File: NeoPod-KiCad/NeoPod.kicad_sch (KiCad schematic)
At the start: 61 parts, among them J1 SJ-3523-SMT-TR, J2 USB4500-03-0-A_REVA1, J4 USB4500-03-0-A_REVA1, Q1 CSD25480F3, SW1 SW_SPST, SW2 SW_SPST, SW3 SW_SPST, SW4 SW_SPST, SW5 SW_SPST, U1 ESP32-WROOM-32, U10 SN74CB3Q3257DBQR, U2 PCM5102A, U3 RP2040, U4 CP2102N-Axx-xQFN24, U5 XC6210B332MR, U6 STC4054GR, U7 TFT_320x240, Y2 40MHz-Xtal

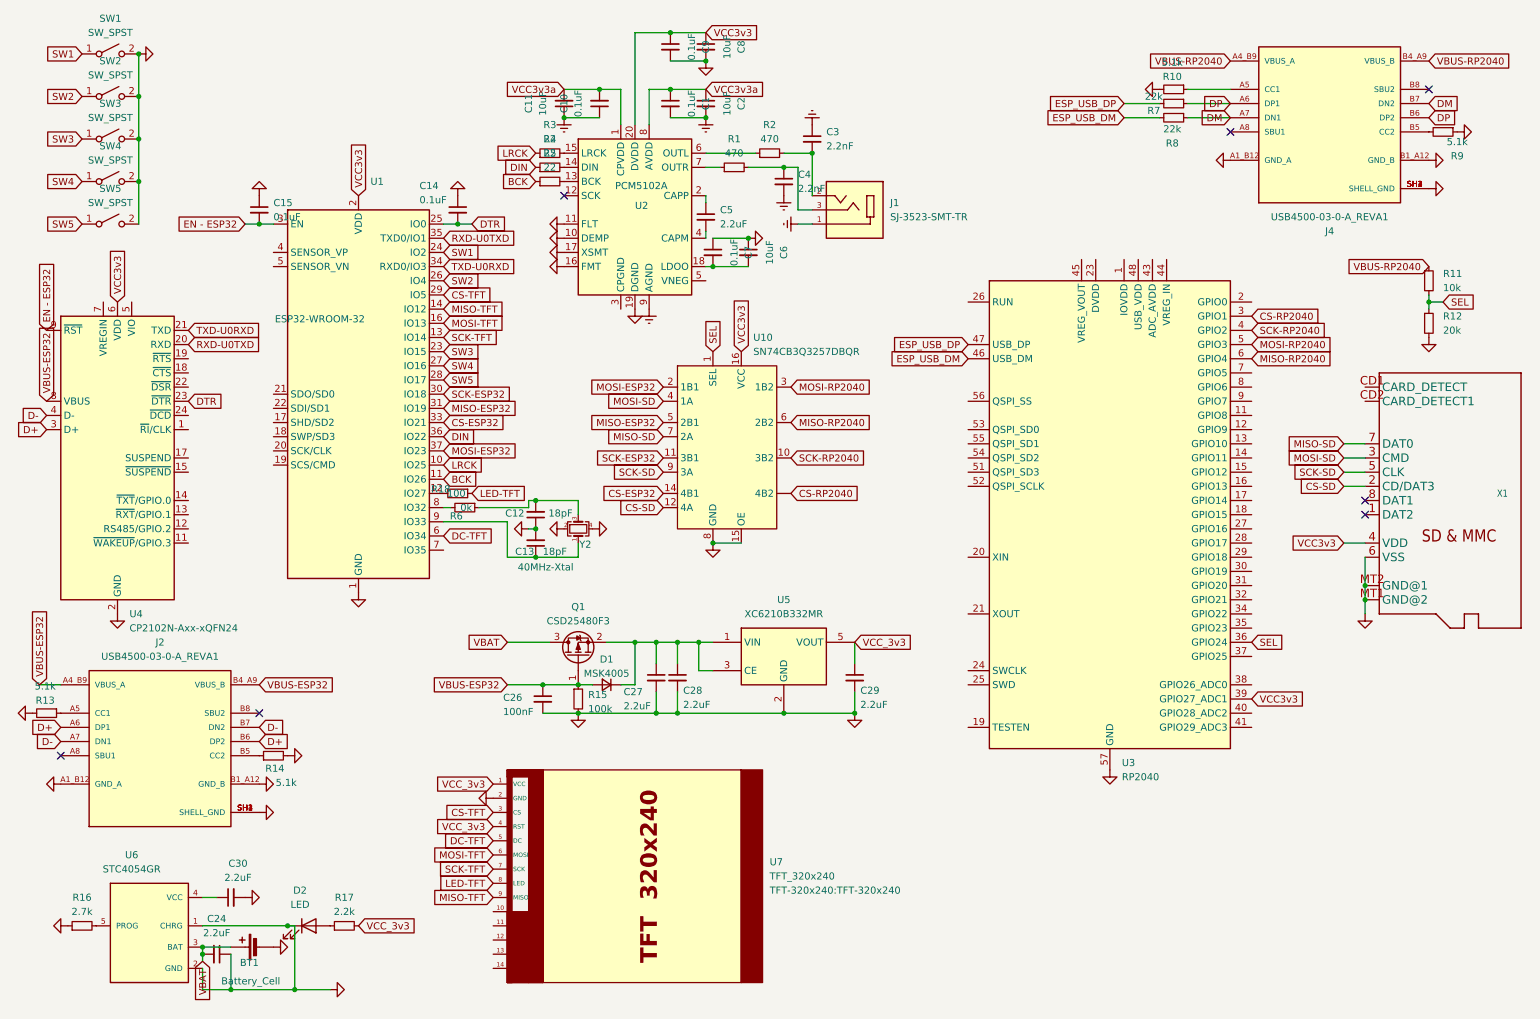
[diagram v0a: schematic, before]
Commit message: Started pcb layout and added images
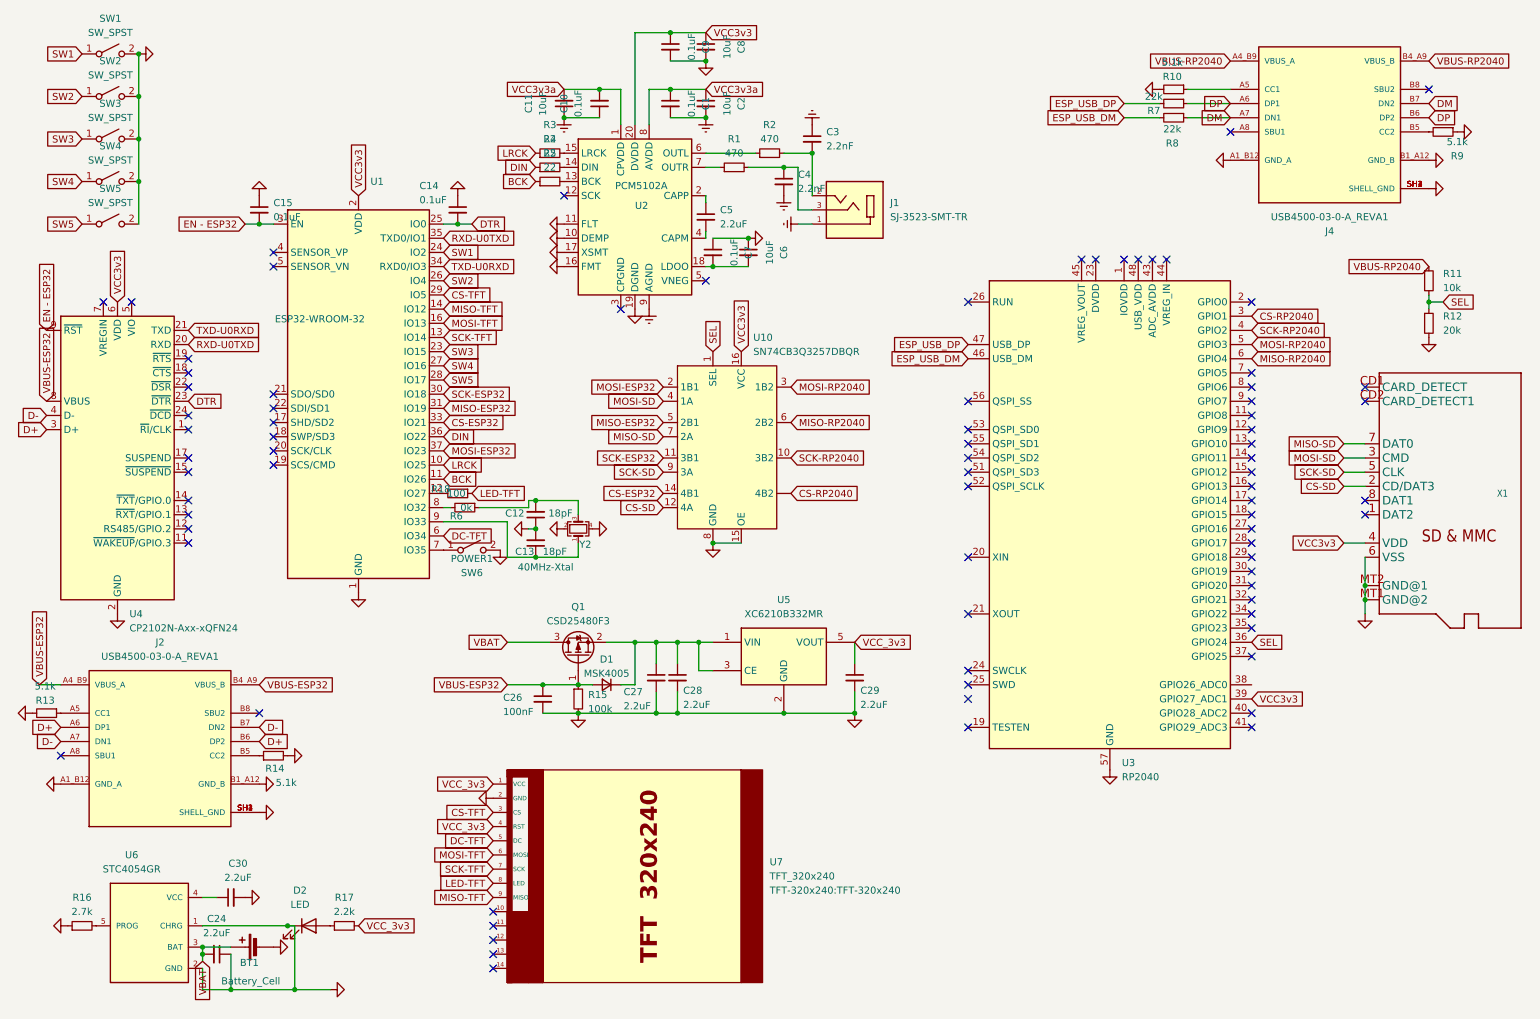
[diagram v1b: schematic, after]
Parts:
- added POWER1: SW6, SW_TS-1088-AR2016:SW_TS-1088-AR02016, symbol Switch:SW_SPST
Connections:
- net AGND: no longer C14.1, C15.1, C6.1, C7.1, J2.A1_B12 (GND_A), J2.B1_A12 (GND_B), J2.SH1 (SHELL_GND), J2.SH2 (SHELL_GND), J2.SH3 (SHELL_GND), J2.SH4 (SHELL_GND), R12.2, SW1.2 (B), SW2.2 (B), SW3.2 (B), SW4.2 (B), SW5.2 (B), U1.1 (GND), U1.15 (GND), U1.38 (GND), U1.39 (GND), U2.10 (DEMP), U2.11 (FLT), U2.16 (FMT), U2.17 (XSMT), U3.57 (GND), U4.2 (GND), U4.25 (GND)
- net GND: now also C14.1, C15.1, C6.1, C7.1, J2.A1_B12 (GND_A), J2.B1_A12 (GND_B), J2.SH1 (SHELL_GND), J2.SH2 (SHELL_GND), J2.SH3 (SHELL_GND), J2.SH4 (SHELL_GND), R12.2, SW1.2 (B), SW2.2 (B), SW3.2 (B), SW4.2 (B), SW5.2 (B), U1.1 (GND), U1.15 (GND), U1.38 (GND), U1.39 (GND), U2.10 (DEMP), U2.11 (FLT), U2.16 (FMT), U2.17 (XSMT), U3.57 (GND), U4.2 (GND), U4.25 (GND), POWER1.2 (B)
- net at U1.7 (IO35): now also POWER1.1 (A)
- no-connect marks 7 -> 79

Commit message: finished pcb
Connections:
- net AGND is gone; now on net GND: C8.2, C9.2, U2.19 (DGND)
- net VCC_3v3 is gone; now on net VCC3v3: C29.1, R17.2, U5.5 (VOUT), U7.1 (VCC), U7.4 (RST)
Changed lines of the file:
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@@
 		)
 	)
+	(global_label "VCC3v3"
+		(shape input)
+		(at 74.93 176.53 0)
+		(fields_autoplaced yes)
+		(effects
+			(font
+				(size 1.27 1.27)
+			)
+			(justify left)
+		)
+		(property "Intersheetrefs" "${INTERSHEET_REFS}"
+			(at 84.9304 176.53 0)
+			(effects
+				(font
+					(size 1.27 1.27)
+				)
+				(justify left)
+				(hide yes)
+			)
+		)
+	)
 	(global_label "VCC3v3a"
 		(shape input)
@@
 		)
 	)
-	(global_label "VCC_3v3"
-		(shape input)
-		(at 163.83 125.73 0)
-		(fields_autoplaced yes)
-		(effects
-			(font
-				(size 1.27 1.27)
-			)
-			(justify left)
-		)
-		(property "Intersheetrefs" "${INTERSHEET_REFS}"
-			(at 174.798 125.73 0)
-			(effects
-				(font
-					(size 1.27 1.27)
-				)
-				(justify left)
-				(hide yes)
-			)
-		)
-	)
 	(global_label "VBUS-ESP32"
 		(shape input)
@@
 		)
 	)
+	(global_label "VCC3v3"
+		(shape input)
+		(at 99.06 158.75 180)
+		(fields_autoplaced yes)
+		(effects
+			(font
+				(size 1.27 1.27)
+			)
+			(justify right)
+		)
+		(property "Intersheetrefs" "${INTERSHEET_REFS}"
+			(at 89.0596 158.75 0)
+			(effects
+				(font
+					(size 1.27 1.27)
+				)
+				(justify right)
+				(hide yes)
+			)
+		)
+	)
 	(global_label "VBAT"
 		(shape input)
@@
 		)
 	)
+	(global_label "VCC3v3"
+		(shape input)
+		(at 99.06 151.13 180)
+		(fields_autoplaced yes)
+		(effects
+			(font
+				(size 1.27 1.27)
+			)
+			(justify right)
+		)
+		(property "Intersheetrefs" "${INTERSHEET_REFS}"
+			(at 89.0596 151.13 0)
+			(effects
+				(font
+					(size 1.27 1.27)
+				)
+				(justify right)
+				(hide yes)
+			)
+		)
+	)
 	(global_label "SW2"
 		(shape input)
@@
 		)
 	)
-	(global_label "VCC_3v3"
-		(shape input)
-		(at 74.93 176.53 0)
-		(fields_autoplaced yes)
-		(effects
-			(font
-				(size 1.27 1.27)
-			)
-			(justify left)
-		)
-		(property "Intersheetrefs" "${INTERSHEET_REFS}"
-			(at 85.898 176.53 0)
-			(effects
-				(font
-					(size 1.27 1.27)
-				)
-				(justify left)
-				(hide yes)
-			)
-		)
-	)
 	(global_label "DP"
 		(shape input)
@@
 		)
 	)
-	(global_label "VCC_3v3"
-		(shape input)
-		(at 99.06 158.75 180)
-		(fields_autoplaced yes)
-		(effects
-			(font
-				(size 1.27 1.27)
-			)
-			(justify right)
-		)
-		(property "Intersheetrefs" "${INTERSHEET_REFS}"
-			(at 88.092 158.75 0)
-			(effects
-				(font
-					(size 1.27 1.27)
-				)
-				(justify right)
-				(hide yes)
-			)
-		)
-	)
 	(global_label "MOSI-SD"
 		(shape input)
@@
 		)
 	)
+	(global_label "VCC3v3"
+		(shape input)
+		(at 163.83 125.73 0)
+		(fields_autoplaced yes)
+		(effects
+			(font
+				(size 1.27 1.27)
+			)
+			(justify left)
+		)
+		(property "Intersheetrefs" "${INTERSHEET_REFS}"
+			(at 173.8304 125.73 0)
+			(effects
+				(font
+					(size 1.27 1.27)
+				)
+				(justify left)
+				(hide yes)
+			)
+		)
+	)
 	(global_label "VBUS-ESP32"
 		(shape input)
@@
 		)
 	)
-	(global_label "VCC_3v3"
-		(shape input)
-		(at 99.06 151.13 180)
-		(fields_autoplaced yes)
-		(effects
-			(font
-				(size 1.27 1.27)
-			)
-			(justify right)
-		)
-		(property "Intersheetrefs" "${INTERSHEET_REFS}"
-			(at 88.092 151.13 0)
-			(effects
-				(font
-					(size 1.27 1.27)
-				)
-				(justify right)
-				(hide yes)
-			)
-		)
-	)
 	(global_label "VCC3v3"
 		(shape input)
@@
 			)
 		)
-		(property "Value" "AGND"
+		(property "Value" "GND"
 			(at 137.16 26.67 0)
 			(effects
@@
 			)
 		)
-		(property "Value" "AGND"
+		(property "Value" "GND"
 			(at 124.46 71.12 0)
 			(effects
